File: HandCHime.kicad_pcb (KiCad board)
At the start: 4 copper layers, 38.1 x 22.6 mm, 18 parts, among them J1 USB_C_Receptacle_USB2.0, J2 Pins, SW0 BOOT, SW1 Row 0, Col 0, SW2 Row 0, Col 1, U1 CH552T, U2 USBLC6-2P6

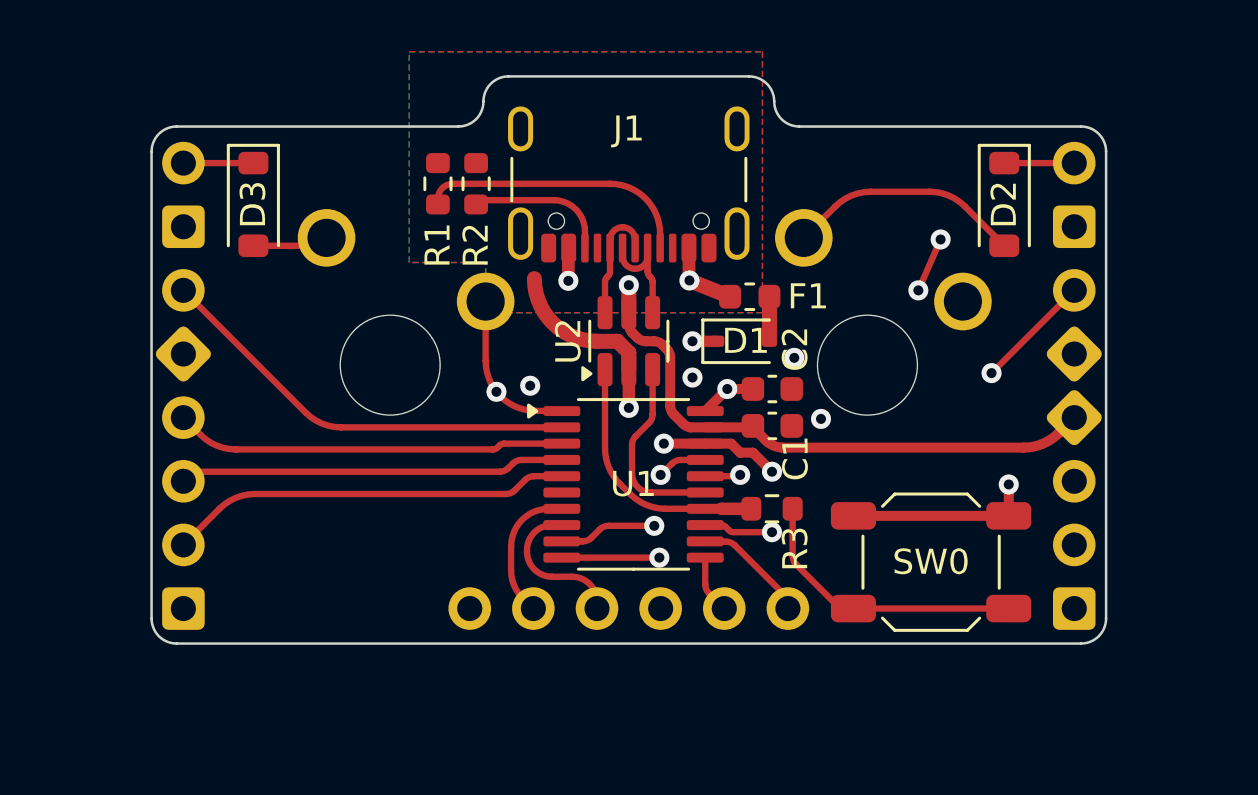
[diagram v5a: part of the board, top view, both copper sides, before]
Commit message: Add notches to bottom left and right corners
This should avoid any supports that might be nearby between switches.
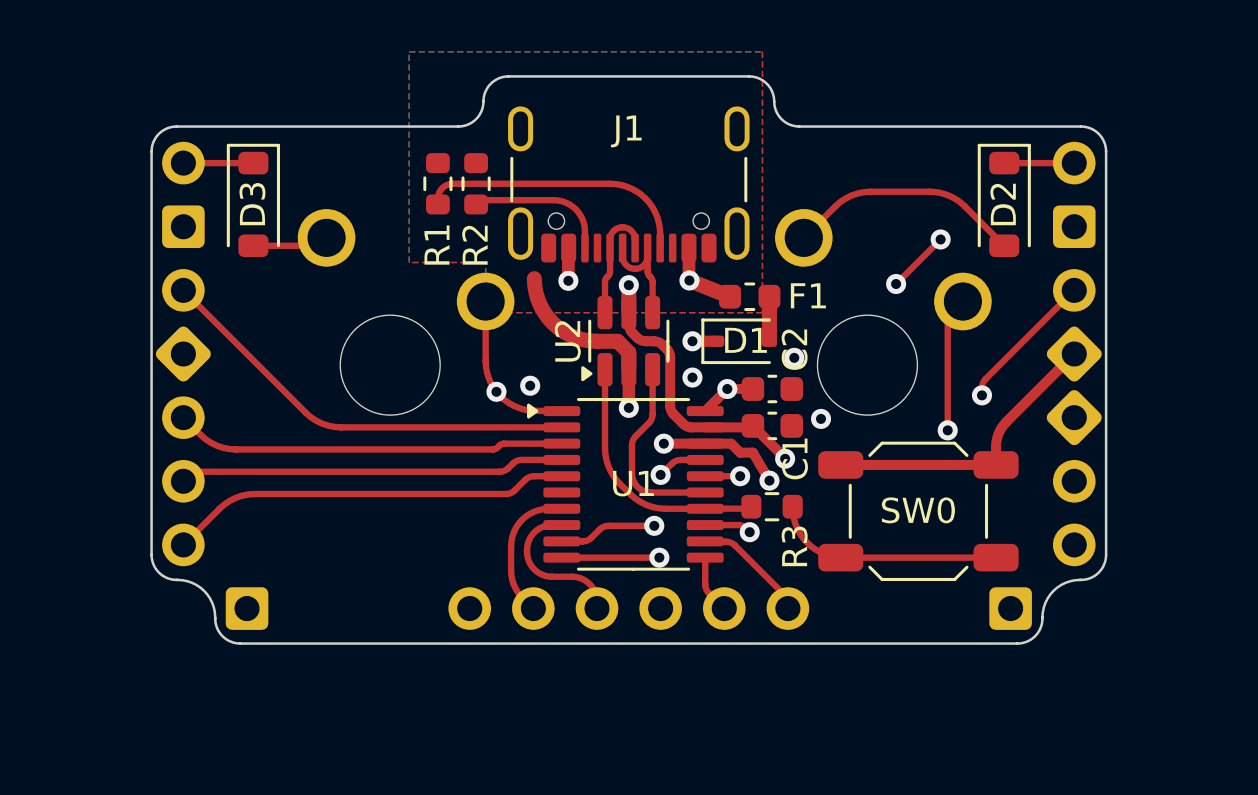
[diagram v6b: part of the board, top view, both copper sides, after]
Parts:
- NT2: footprint NetTie:NetTie-2_SMD_Pad0.5mm -> Project Library:NetTie-2_SMD_Pad0.254mm
- moved SW0 2.09 mm to (170.3, 55.0)
- moved R3 0.08 mm to (164.5, 54.9)
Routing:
- net VCC: track 26.4 -> 29.1 mm, vias 2 -> 3
- net +3V3: track 58.2 -> 56.5 mm, vias 2 -> 1
- net Net-(R3-Pad2): track 10.9 -> 9.50 mm
- net P35: track 20.9 -> 21.4 mm
- net C0: track 33.5 -> 34.0 mm, vias 0 -> 1
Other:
- outline, holes or cut-outs redrawn
- board text added: "bgkendall"
- board text added: "by"
- board text added: "v1.0"
- board text removed: "v1.0 by bgkendall"

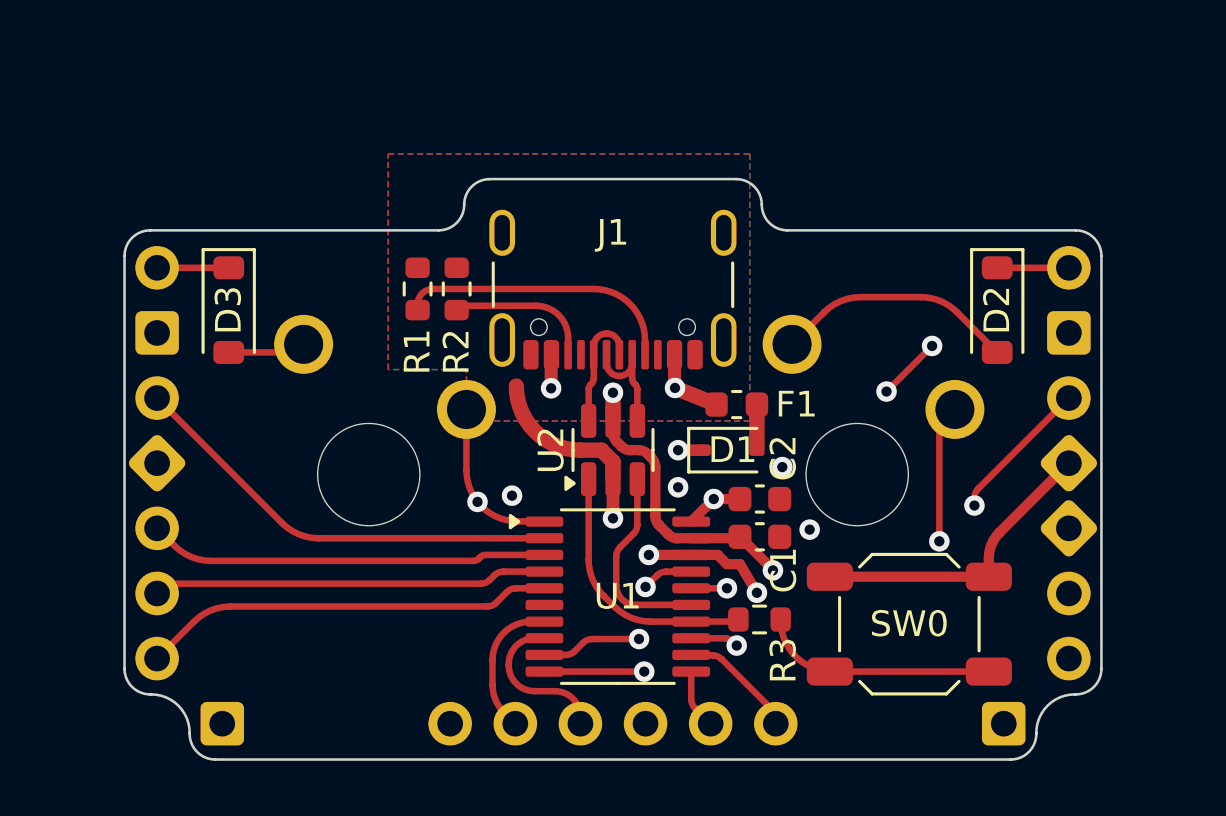
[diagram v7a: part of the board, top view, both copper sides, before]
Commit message: Move switches to centre of board
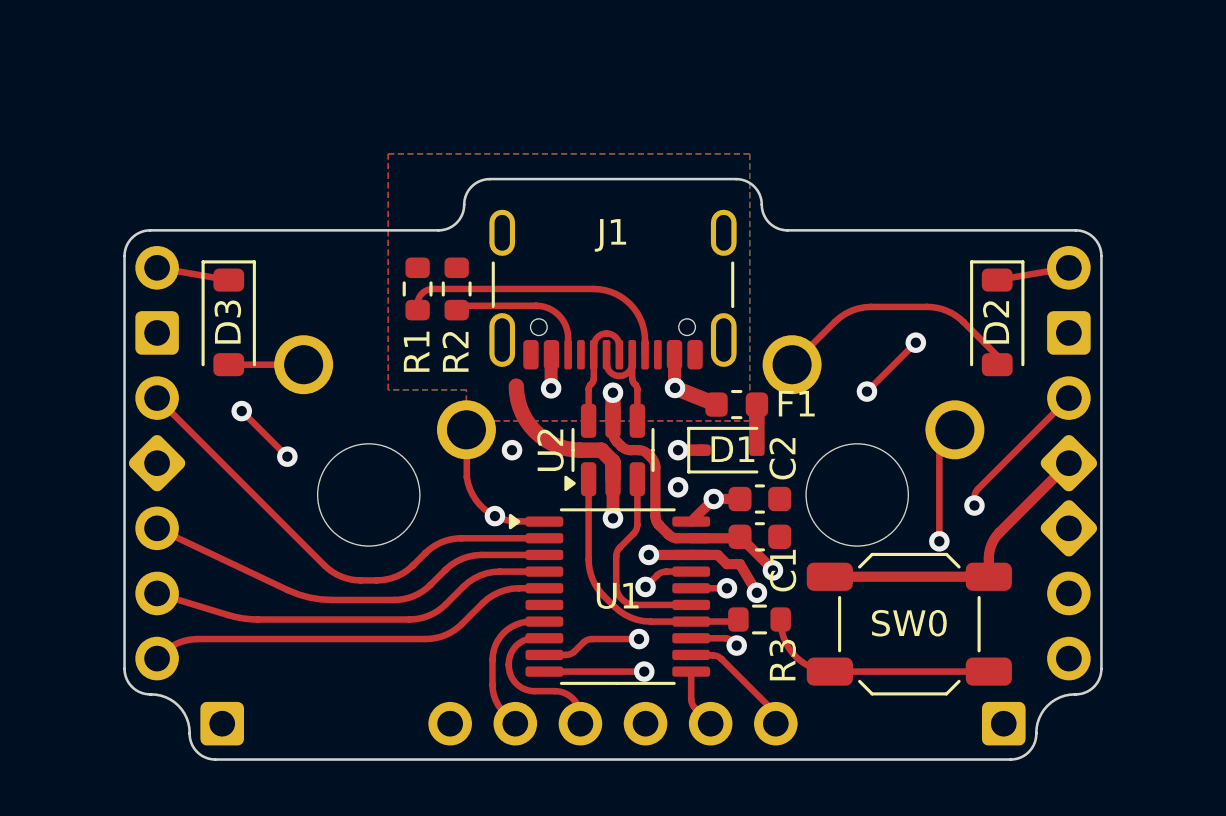
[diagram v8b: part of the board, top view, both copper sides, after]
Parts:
- moved SW1 0.79 mm to (168.3, 50.0)
- moved SW2 0.79 mm to (149.2, 50.0)
- moved D2 0.48 mm to (173.7, 43.3)
- moved D3 0.48 mm to (143.8, 43.3)
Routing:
- net R0: track 65.3 -> 59.3 mm, vias 3 -> 5
- net P14: track 17.3 -> 18.4 mm
- net P16: track 14.7 -> 15.8 mm
- net C0: track 34.0 -> 32.8 mm
- net C1: track 15.6 -> 14.5 mm
- net +3V3: track 56.5 -> 55.8 mm
- net P15: track 15.6 -> 16.2 mm
- net GND: vias 7 -> 5
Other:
- board text added: "v1.0 • bgkendall"
- board text removed: "bgkendall"
- board text removed: "by"
- board text removed: "v1.0"
